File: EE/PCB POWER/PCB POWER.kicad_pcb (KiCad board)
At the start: 2 copper layers, 84 x 84 mm, 48 parts, among them J14 B2B-PH-K-S, J15 B2B-PH-K-S, J16 B2B-PH-K-S, J17 B5B-PH-K-S, J2 1752104, J3 1752104, J5 B2B-PH-K-S, Q1 IPD30N08S2L21ATMA1, Q2 IPD30N08S2L21ATMA1, U1 MIC4427YM-TR, U2 742792510, U3 RPM5.0-6.0, U4 DRV8220DRLR

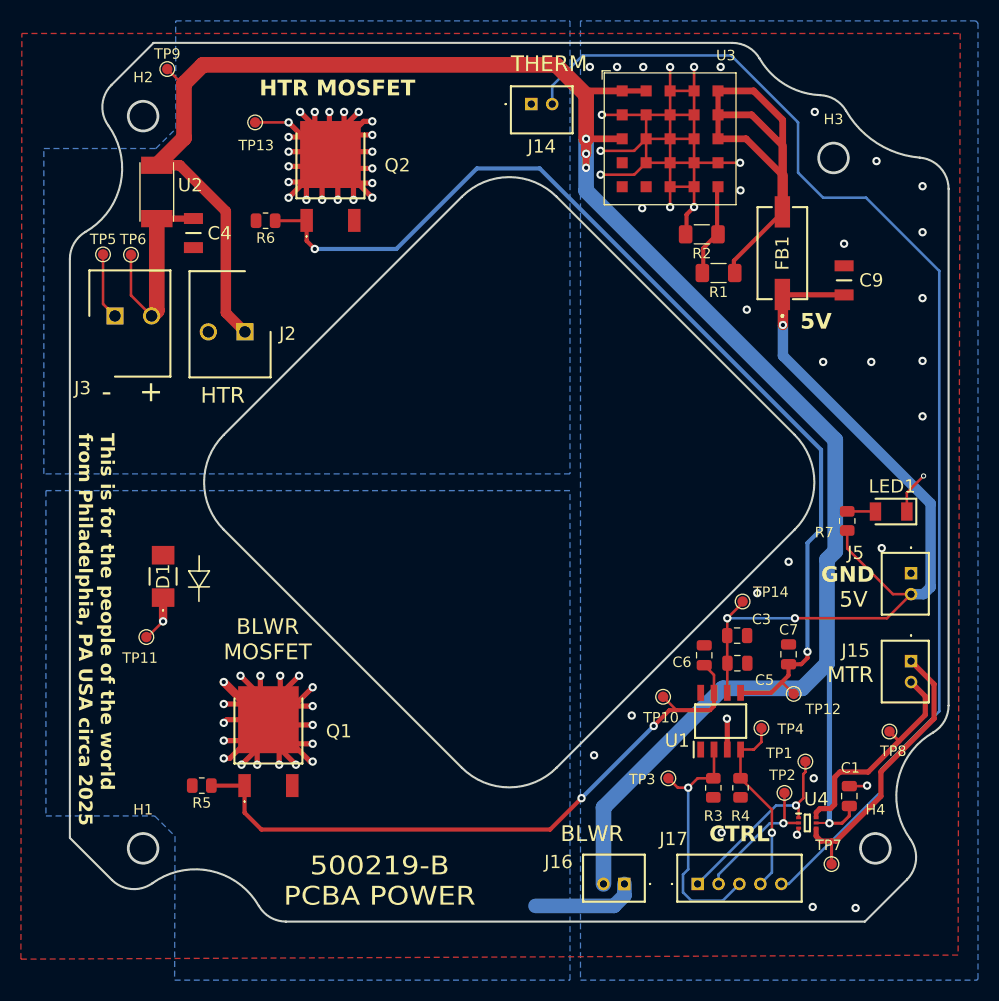
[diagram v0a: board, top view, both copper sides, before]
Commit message: Replace PCB Power with the backup from Tom's zip file + replace all library links to consolidated library
Hopefully everything links now. I also cleaned up the graphics so all the footprint references in the silkscreen are the same size.
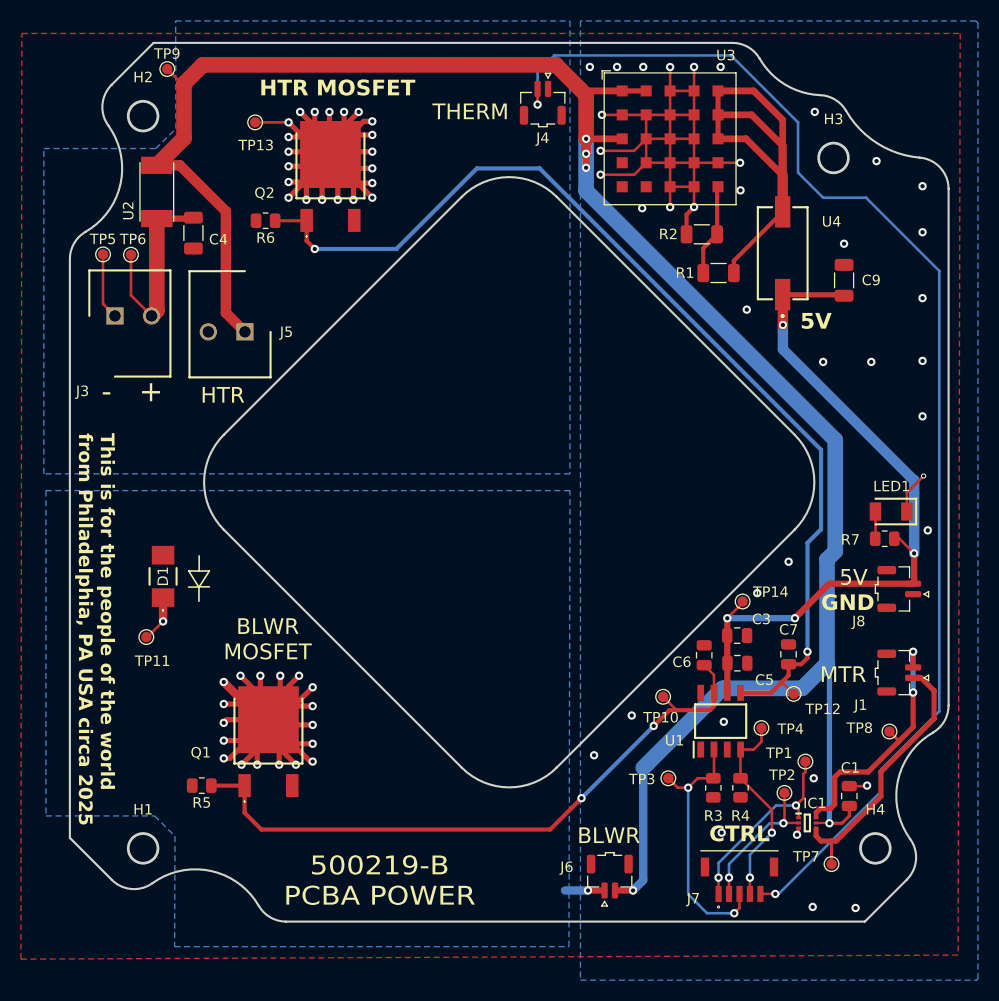
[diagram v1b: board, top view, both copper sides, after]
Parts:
- removed FB1: 7427932, DaisyBio_Mira:7427932
- removed J14, J15, J16: B2B-PH-K-S, DaisyBio_Mira:B2BPHKS
- removed J17: B5B-PH-K-S, DaisyBio_Mira:B5BPHKS
- removed J2: 1752104, DaisyBio_Mira:SHDR2W90P0X350_1X2_760X1000X1255P
- added IC1: DRV8220DRLR, DaisyBio_Mira:SOTFL50P160X60-6N, F.Cu at (128.5, 132.6)
- added J1: T1M-02-F-SV-L-P, Connector_Samtec_MicroMate:Samtec_T1M-02-X-S-V_1x02-1MP_P1.0mm_Terminal_Vertical, F.Cu at (136.7, 118.2)
- added J4: T1M-02-F-SV-L-P, Connector_Samtec_MicroMate:Samtec_T1M-02-X-S-V_1x02-1MP_P1.0mm_Terminal_Vertical, F.Cu at (103.2, 64.3)
- added J6: T1M-02-F-SV-L-P, Connector_Samtec_MicroMate:Samtec_T1M-02-X-S-V_1x02-1MP_P1.0mm_Terminal_Vertical, F.Cu at (109.6, 137.1)
- added J7: T1M-05-F-SV-L, DaisyBio_Mira:T1M-05-X-SV-L-Y, F.Cu at (122.0, 139.4)
- added J8: T1M-02-F-SV-L-P, Connector_Samtec_MicroMate:Samtec_T1M-02-X-S-V_1x02-1MP_P1.0mm_Terminal_Vertical, F.Cu at (136.7, 110.2)
- C4, C9: footprint DaisyBio_Mira:CAPC3216X180N -> Capacitor_SMD:C_1206_3216Metric
- J5: value B2B-PH-K-S -> 1752104; footprint DaisyBio_Mira:B2BPHKS -> DaisyBio_Mira:SHDR2W90P0X350_1X2_760X1000X1255P
- R1, R2: footprint Resistor_SMD:R_1206_3216Metric_Pad1.30x1.75mm_HandSolder -> Resistor_SMD:R_1206_3216Metric
- U4: value DRV8220DRLR -> 7427932; footprint DaisyBio_Mira:SOTFL50P160X60-6N -> DaisyBio_Mira:7427932
- moved J5 67.7 mm to (74.7, 85.6), turned to 180 degrees
- moved U4 54.5 mm to (126.1, 78.1), turned to 90 degrees
- moved R7 3.97 mm to (135.9, 105.4), turned to 180 degrees
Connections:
- C1 pad 2: Net-(J16-Pin_2) -> Net-(IC1-VM)
- C3 pad 1: Net-(J5-Pin_2) -> Net-(J8-Pin_2)
- C5 pad 1: Net-(J5-Pin_2) -> Net-(J8-Pin_2)
- C9 pad 2: Net-(J5-Pin_2) -> Net-(J8-Pin_2)
- J5 pad 1: GND -> Net-(IC1-VM)
- Q2 pad 2: Net-(J2-Pin_2) -> Net-(J5-Pin_2)
- R7 pad 1: Net-(J5-Pin_2) -> Net-(J8-Pin_2)
- TP13 pad 1: Net-(J2-Pin_2) -> Net-(J5-Pin_2)
- TP14 pad 1: Net-(J5-Pin_2) -> Net-(J8-Pin_2)
- TP9 pad 1: Net-(J16-Pin_2) -> Net-(IC1-VM)
- U1 pad 6: Net-(J5-Pin_2) -> Net-(J8-Pin_2)
- U2 pad 2: Net-(J16-Pin_2) -> Net-(IC1-VM)
- U3 pad A1: Net-(J16-Pin_2) -> Net-(IC1-VM)
- U3 pad A2: Net-(J16-Pin_2) -> Net-(IC1-VM)
- U3 pad C1: Net-(J16-Pin_2) -> Net-(IC1-VM)
- U4 pad 1: MTR_PID1 -> Net-(J8-Pin_2)
- U4 pad 2: MTR_PID2 -> Net-(U3-Sense)
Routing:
- net Net-(IC1-VM): track 0.00 -> 204.9 mm, vias 0 -> 5
- net Net-(J16-Pin_2): track 203.7 -> 0.00 mm, vias 4 -> 0
- net Net-(J2-Pin_2): track 106.5 -> 0.00 mm, vias 21 -> 0
- net Net-(J8-Pin_2): track 0.00 -> 69.7 mm, vias 0 -> 4
- net Net-(J5-Pin_2): track 79.3 -> 106.5 mm, vias 3 -> 21
- net Net-(D1-K): track 110.2 -> 103.9 mm, vias 19 -> 20
- net THERM: track 116.6 -> 122.7 mm, vias 0 -> 2
- net MTR_1: track 21.2 -> 24.8 mm, vias 0 -> 2
- net GND: track 86.8 -> 83.8 mm
- net HTR_PID: track 18.4 -> 19.7 mm, vias 1 -> 2
- net MTR_2: track 27.0 -> 25.7 mm
- net BLWR_PID: track 24.4 -> 25.2 mm, vias 1 -> 2
- net MTR_PID2: track 13.5 -> 14.1 mm, vias 1 -> 2
- net MTR_PID1: track 18.4 -> 18.5 mm, vias 1 -> 2
- added copper zone on B.Cu, net Net-(J5-Pin_2)
- removed copper zone on B.Cu, net Net-(J2-Pin_2)
